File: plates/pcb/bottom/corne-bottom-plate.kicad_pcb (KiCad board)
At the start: 2 copper layers, 133.8 x 91.4 mm, 7 parts

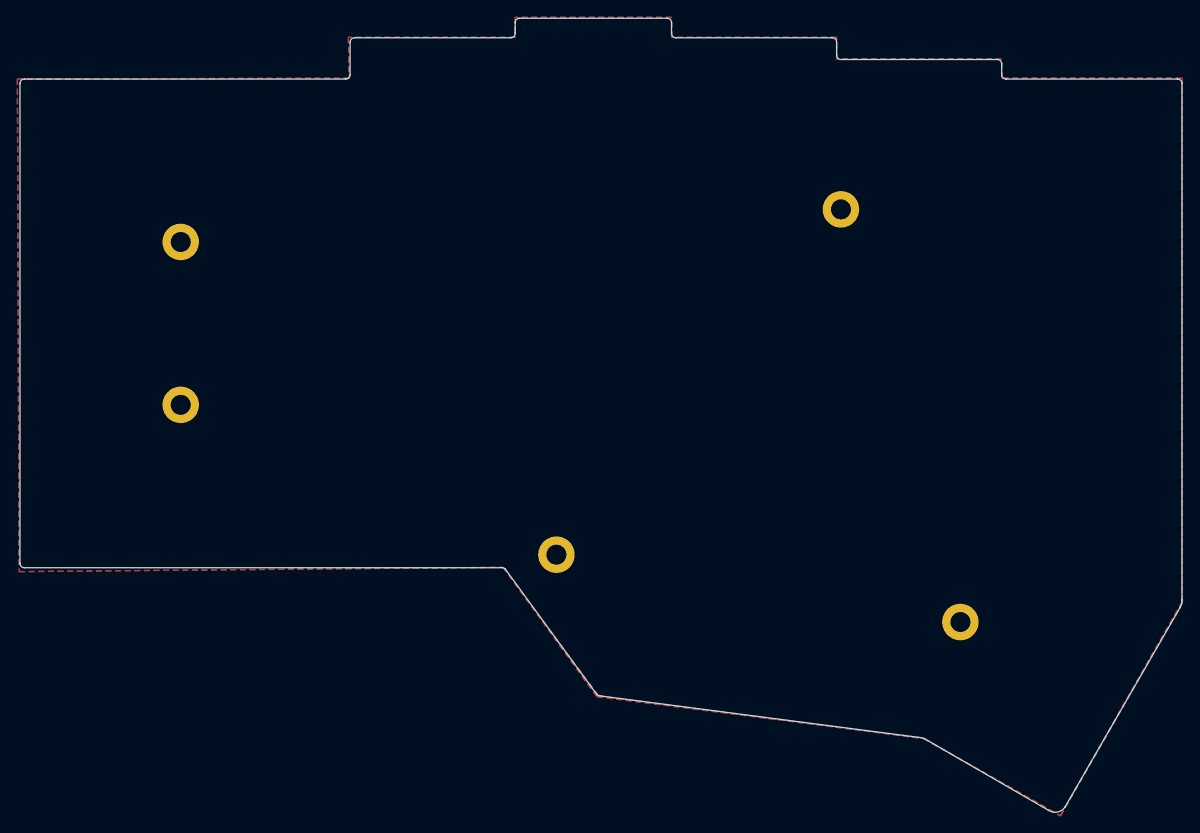
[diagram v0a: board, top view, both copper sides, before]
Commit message: Bottom plate honeycomb design
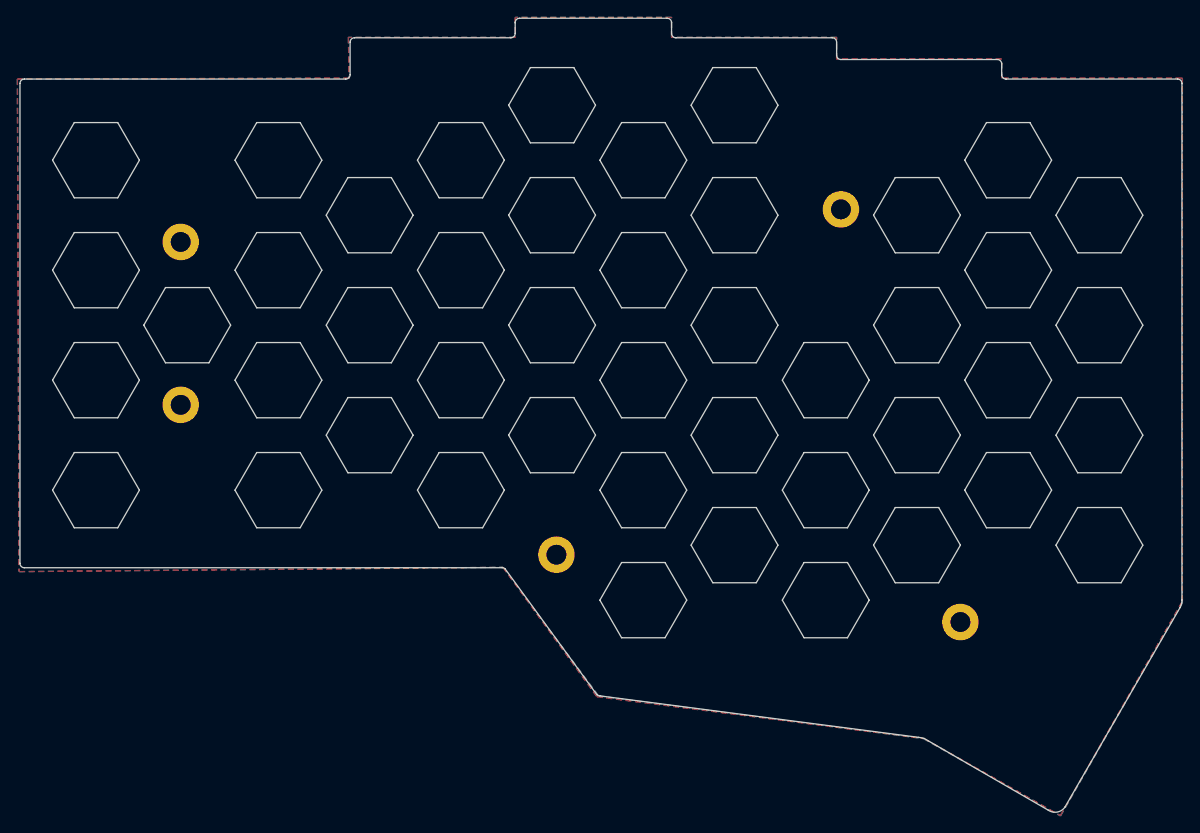
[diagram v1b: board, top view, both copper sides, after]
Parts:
- removed G*** (x2): LOGO, kbd:corne-horizontal
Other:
- outline, holes or cut-outs redrawn
- net class Default removed

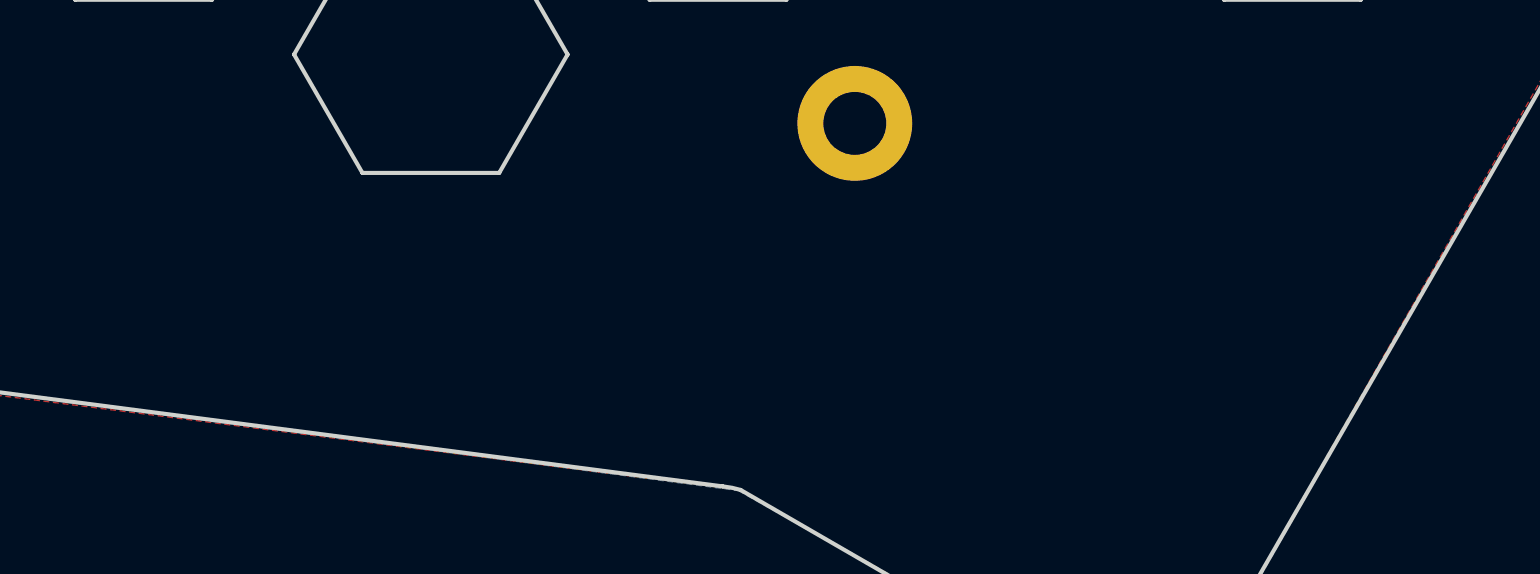
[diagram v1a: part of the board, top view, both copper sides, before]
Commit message: Bottom plate VersaKomb design
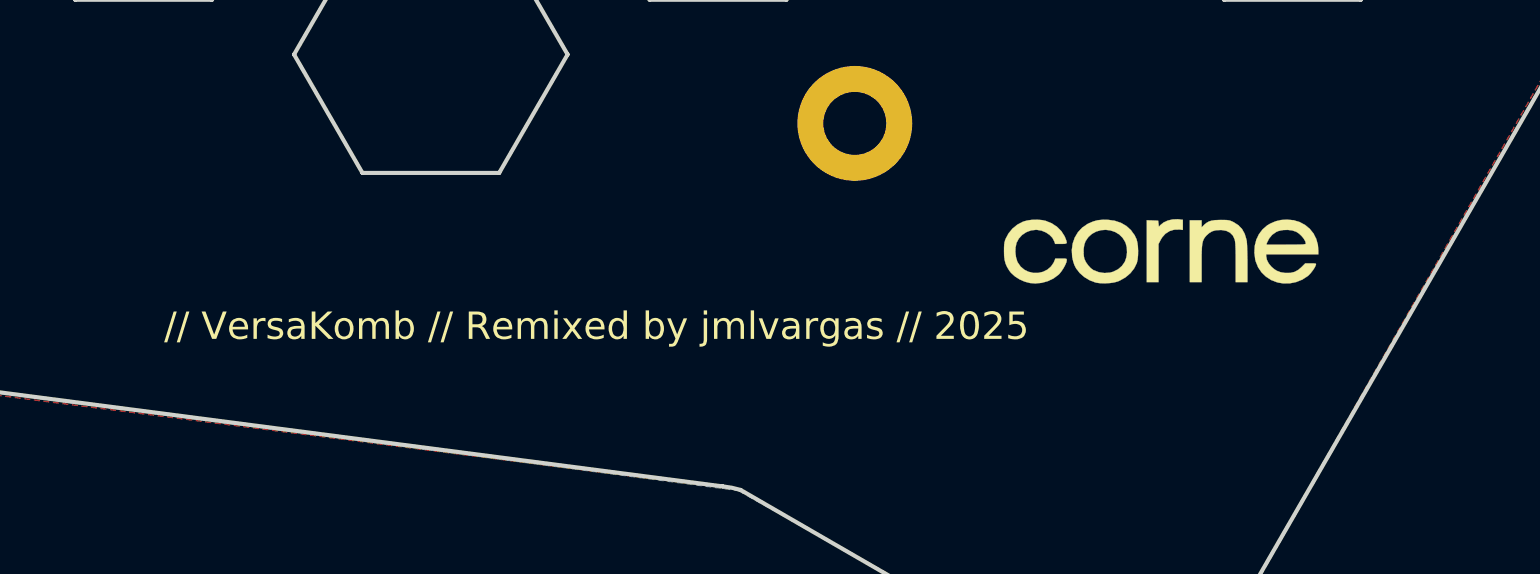
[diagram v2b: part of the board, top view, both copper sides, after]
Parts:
- added G***: LOGO, kbd:corne-logo-horizontal, F.Cu at (180.6, 135.3)
- added G***: LOGO, kbd:corne-logo-horizontal, B.Cu at (180.6, 135.3)
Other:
- board text added: "// VersaKomb // Remixed by jmlvargas // 2025"

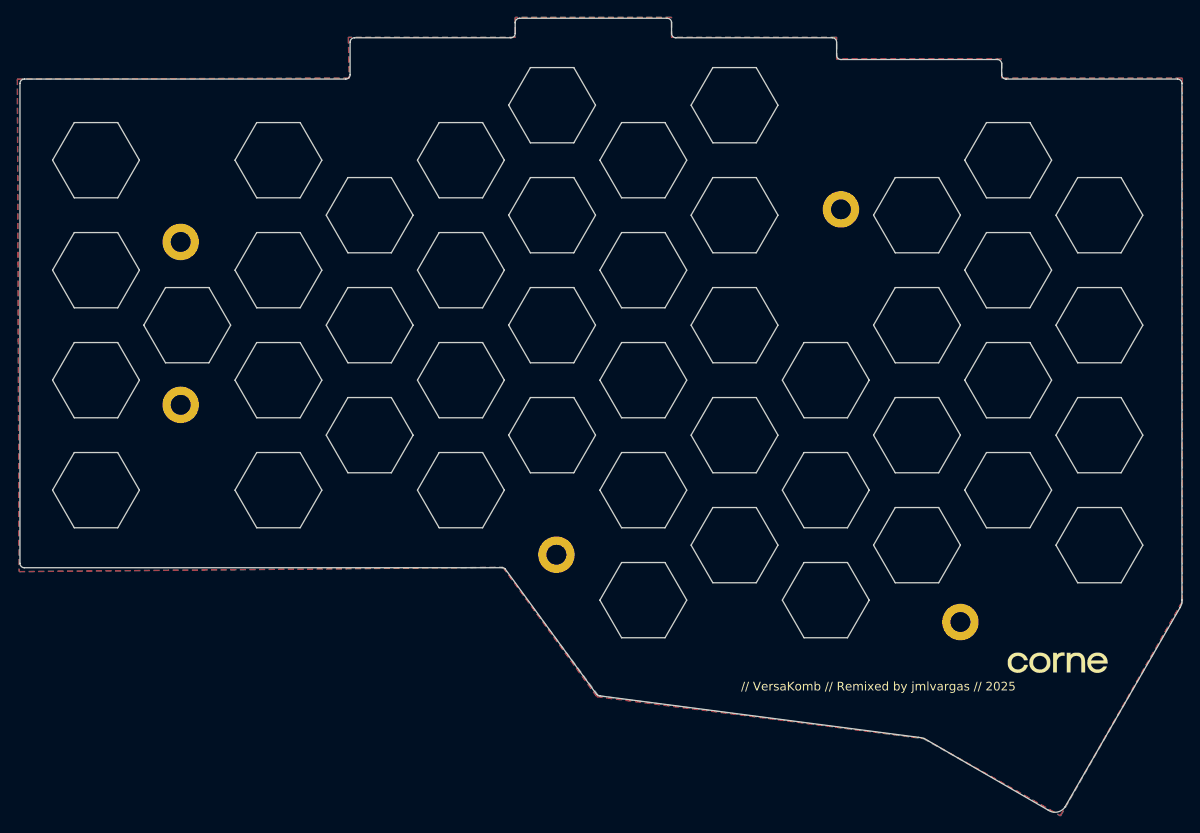
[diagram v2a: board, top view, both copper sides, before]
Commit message: Bottom plate VersaKomb design
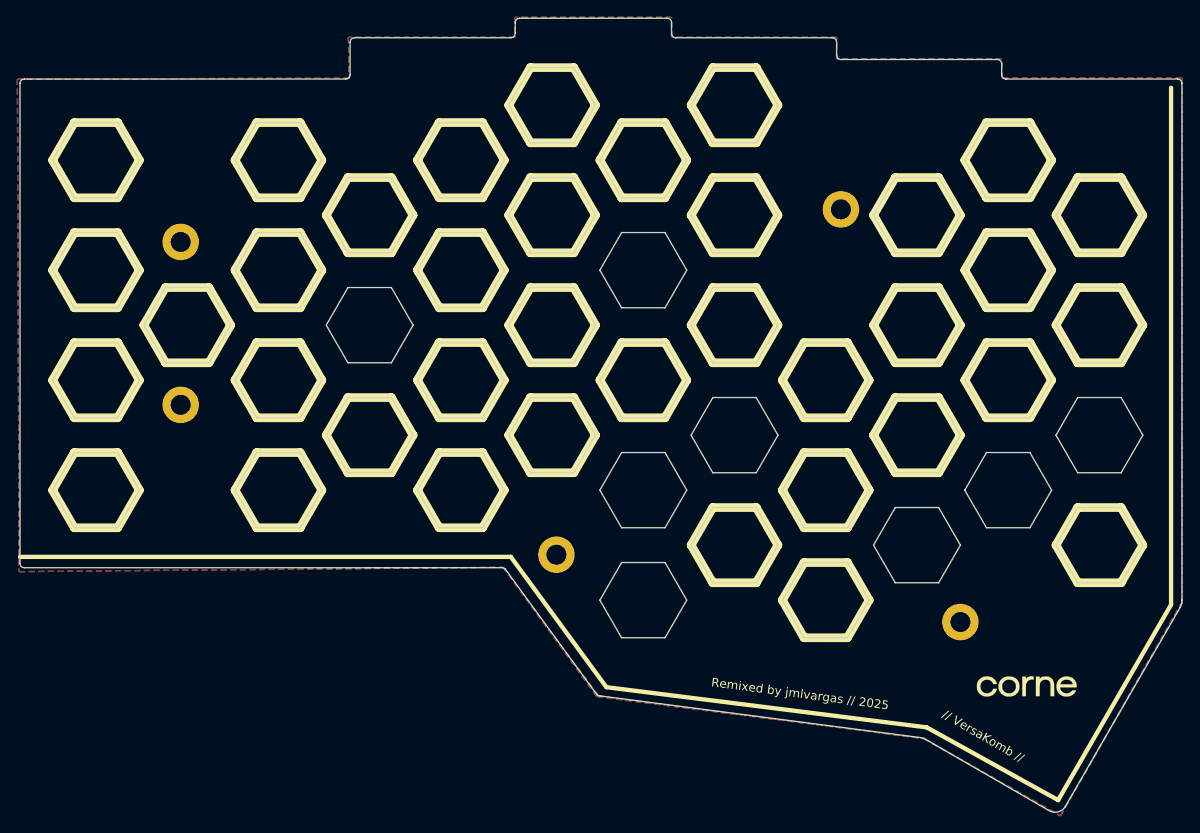
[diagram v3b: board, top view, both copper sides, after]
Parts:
- G***: moved to F.Cu
- G***: moved to B.Cu
- moved G*** 4.49 mm to (177.0, 138.0), turned to 0 degrees
- moved G*** 4.49 mm to (177.0, 138.0), turned to 180 degrees
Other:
- outline, holes or cut-outs redrawn
- board text added: "// VersaKomb //"
- board text added: "Remixed by jmlvargas // 2025"
- board text removed: "// VersaKomb // Remixed by jmlvargas // 2025"

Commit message: Bottom plate, space for rubber feet
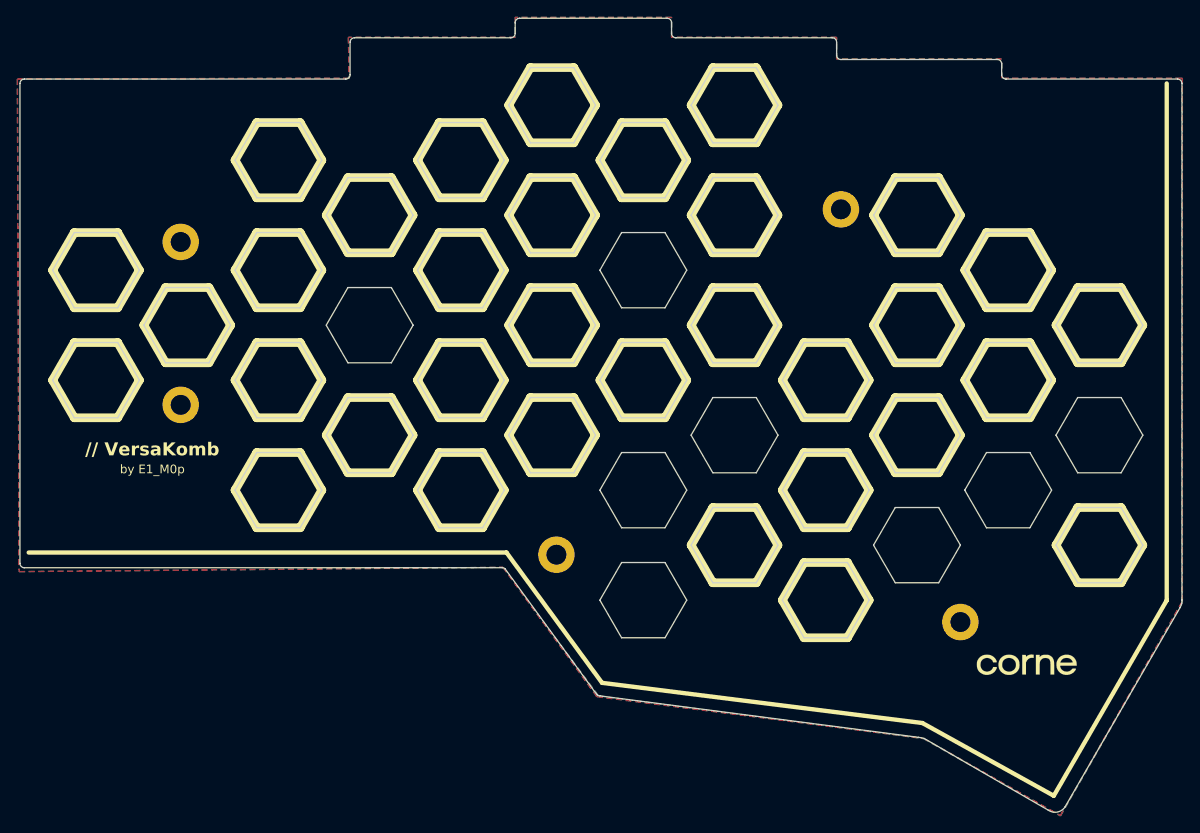
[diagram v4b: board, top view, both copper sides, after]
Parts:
- moved G*** 2.50 mm to (177.0, 135.5) (x2)
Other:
- outline, holes or cut-outs redrawn
- board text added: "// VersaKomb"
- board text added: "by E1_M0p"
- board text removed: "// VersaKomb //"
- board text removed: "Remixed by jmlvargas // 2025"

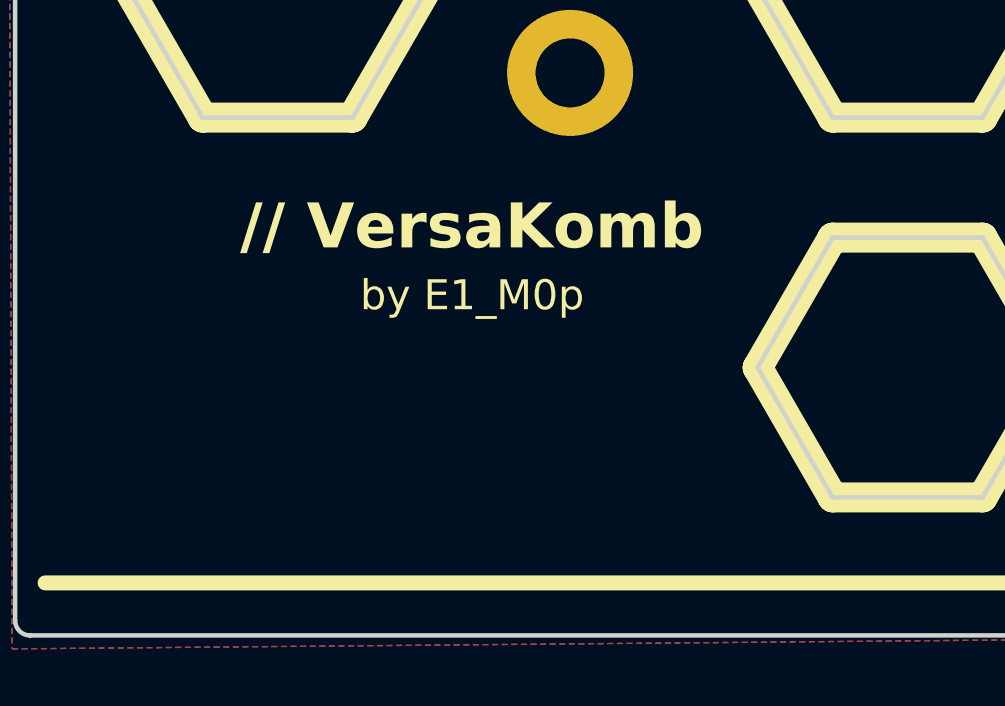
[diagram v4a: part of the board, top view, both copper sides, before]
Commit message: Logo relocated
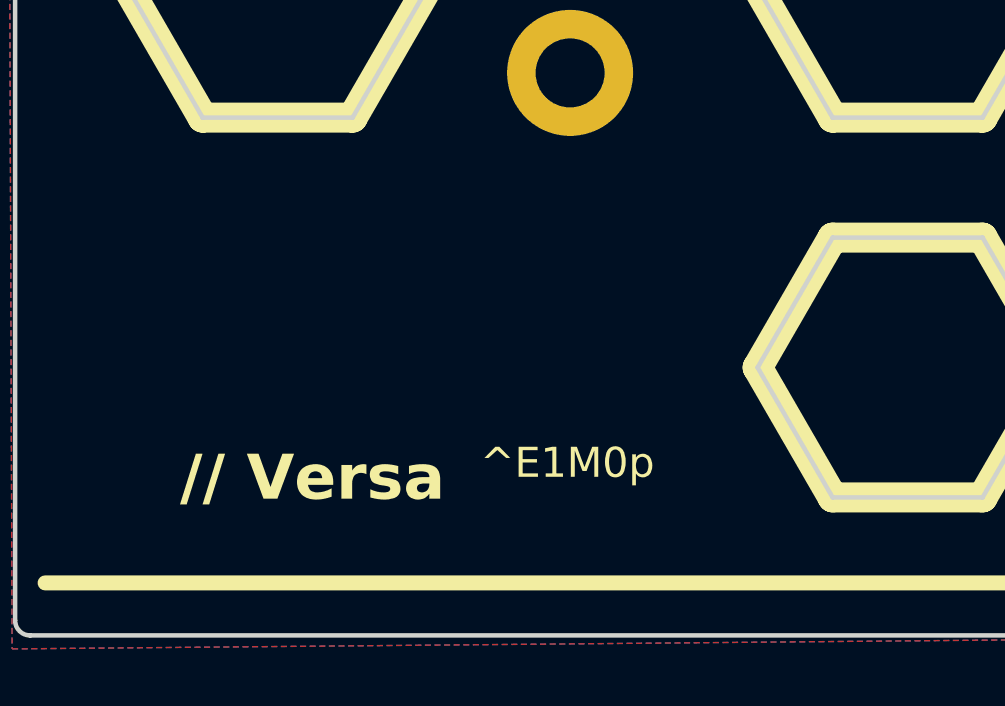
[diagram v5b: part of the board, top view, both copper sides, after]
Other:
- board text added: "// Versa"
- board text added: "^E1M0p"
- board text removed: "// VersaKomb"
- board text removed: "by E1_M0p"
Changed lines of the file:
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@@
 		(layer "F.Fab")
 	)
-	(gr_text "by E1_M0p"
-		(at 80.5 113.5 0)
+	(gr_text "// Versa"
+		(at 82.003571 119 -0)
+		(layer "B.SilkS")
+		(effects
+			(font
+				(size 1.5 1.5)
+				(thickness 0.3)
+				(bold yes)
+			)
+			(justify left mirror)
+		)
+	)
+	(gr_text "^E1M0p"
+		(at 72 118.5 -0)
 		(layer "B.SilkS")
 		(effects
 			(font
 				(size 1 1)
-				(thickness 0.15)
-			)
-			(justify left bottom mirror)
-		)
-	)
-	(gr_text "// VersaKomb"
-		(at 85 111.5 0)
-		(layer "B.SilkS")
-		(effects
-			(font
-				(size 1.5 1.5)
-				(thickness 0.2)
-				(bold yes)
-			)
-			(justify left bottom mirror)
-		)
-	)
-	(gr_text "// VersaKomb"
-		(at 68.5 111.5 -0)
+				(thickness 0.125)
+			)
+			(justify left mirror)
+		)
+	)
+	(gr_text "// Versa"
+		(at 66.496429 119 0)
 		(layer "F.SilkS")
 		(effects
 			(font
 				(size 1.5 1.5)
-				(thickness 0.2)
+				(thickness 0.3)
 				(bold yes)
 			)
-			(justify left bottom)
-		)
-	)
-	(gr_text "by E1_M0p"
-		(at 72.5 113.5 -0)
+			(justify left)
+		)
+	)
+	(gr_text "^E1M0p"
+		(at 76.5 118.5 0)
 		(layer "F.SilkS")
 		(effects
 			(font
 				(size 1 1)
-				(thickness 0.15)
-			)
-			(justify left bottom)
+				(thickness 0.125)
+			)
+			(justify left)
 		)
 	)
@@
 	)
 	(group ""
+		(members "3493de1e-518c-4b16-abbd-a06ca3a4c6cd" "a83e21fd-b8ad-4aa5-83a9-dff7bbfd107f")
+	)
+	(group ""
 		(members "11d5b2b3-0d6d-4f89-8e18-14432dc425e3" "a2f5c833-23c5-4cc1-847b-c471e32b44a8"
 			"acb7eb08-c3c8-4f61-b3f8-086e56820520" "b1ef34c8-ad7c-4266-af37-dd325a9c50dc"
@@
 	)
 	(group ""
+		(members "2f222c44-c136-4a50-91a9-8f9402699df8" "30c79a17-9dc1-4aca-bd8a-df8e463e2d42")
+	)
+	(group ""
